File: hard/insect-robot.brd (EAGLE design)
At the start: 10.2 x 25.4 mm, 13 parts, among them Q1 AO3400, SW1 SWITCH-DT, U1 ATMEGA328P-QFN32, U2 PW0316

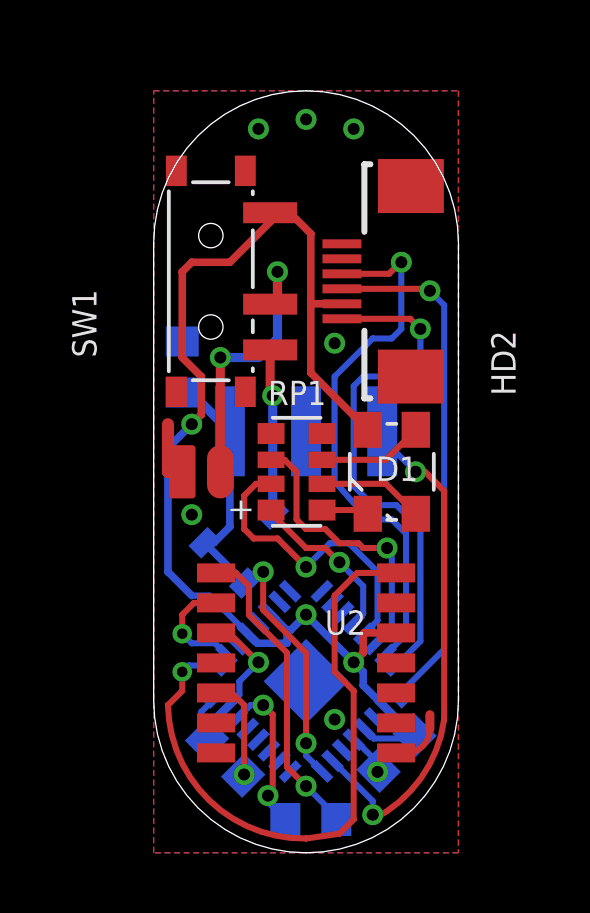
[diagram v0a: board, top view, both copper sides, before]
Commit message: Relocate some components
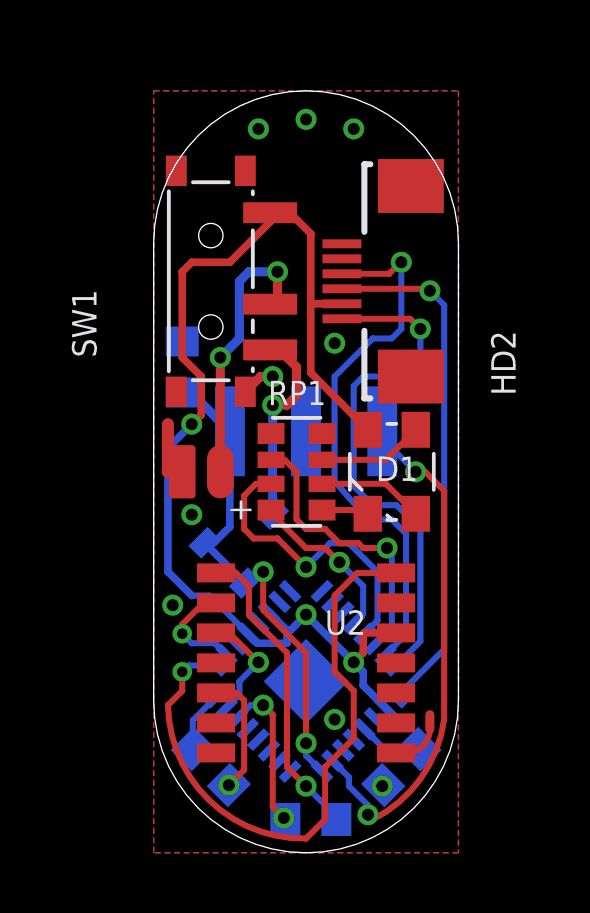
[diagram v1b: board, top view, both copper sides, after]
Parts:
- moved R2 0.57 mm to (1.91, 2.86)
- moved C1 0.50 mm to (8.26, 2.86)
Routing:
- net SWITCH-B: track 5.71 -> 6.83 mm
- net R-BCTS: track 3.51 -> 4.07 mm
- net LINK: track 21.2 -> 20.7 mm
- net GND: track 5.65 -> 5.44 mm, vias 7 -> 9

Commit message: Redesign
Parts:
- removed Q1: AO3400, MyLibrary:SOT23-0
- removed R3: 1kΩ, MyLibrary:SMD0603
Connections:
- removed net BAT-COM: BAT1.+, SW1.COM
- removed net SWITCH-B: Q1.3, SW1.B
- new net RST: HD2.5, U1.29
- new net VDD: D1.2, SW1.A, U1.18, U1.4, U1.6, U2.5
- net GND: no longer R3.2
- net L: now also HD1.1, U1.24; no longer HD1.3, U1.23
- net R: now also HD1.3, U1.23; no longer HD1.1, Q1.1, Q1.2, R3.1, U1.24
- net VBAT: now also BAT1.+, SW1.COM; no longer D1.2, SW1.A, U1.18, U1.4, U1.6, U2.5
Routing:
- net VDD: track 0.00 -> 37.2 mm, vias 0 -> 4
- net VBAT: track 38.2 -> 9.20 mm, vias 3 -> 2
- net BAT-COM: track 9.20 -> 0.00 mm, vias 2 -> 0
- net SWITCH-B: track 6.83 -> 0.00 mm, vias 1 -> 0
- net L: track 17.2 -> 12.6 mm
- net MISO: track 17.5 -> 14.6 mm
- net R: track 16.5 -> 17.9 mm
- net GND: track 5.44 -> 4.31 mm, vias 9 -> 7

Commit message: Redesign finished
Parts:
- D1: value LED-RGB-A-3528 -> LED-RGB-A-0603; device MyLibrary:3528-4 -> MyLibrary:LED-0603X2
- moved D1 11.5 mm to (5.08, 23.8)
- moved RP1 0.63 mm to (5.40, 12.7), turned to 0 degrees
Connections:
- net B-: now also D1.4, RP1.7; no longer D1.3, RP1.3
- net G-: now also D1.2; no longer D1.4
- net R-: now also RP1.3; no longer RP1.7
- net RB-: now also RP1.8; no longer RP1.4
- net RR-: now also RP1.4; no longer RP1.8
- net VDD: now also D1.3; no longer D1.2
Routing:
- net RST: track 0.00 -> 27.9 mm, vias 0 -> 3
- net R-: track 1.81 -> 11.5 mm, vias 0 -> 2
- net G-: track 3.54 -> 12.3 mm, vias 0 -> 2
- net B-: track 3.54 -> 11.3 mm, vias 0 -> 2
- net VDD: track 37.2 -> 32.1 mm
- net RG-: track 10.1 -> 6.29 mm
- net RB-: track 9.52 -> 6.60 mm
- net VBAT: track 9.20 -> 11.6 mm
- net MOSI: track 17.8 -> 16.4 mm
- net L: track 12.6 -> 13.7 mm
- net R-TX: track 10.6 -> 11.5 mm
- net R: track 17.9 -> 18.6 mm
- net GND: vias 7 -> 6

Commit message: Place labels
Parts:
- added OSHW: (no value), MyLibrary:ICON-OSHW
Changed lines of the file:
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@@
 </element>
 <element name="D1" library="MyLibrary" package="LED-0603X2" value="LED-RGB-A-0603" x="5.08" y="23.8125" smashed="yes" rot="R270">
-<attribute name="NAME" x="7.6075" y="23.9175" size="0.8128" layer="25" font="vector" rot="R90"/>
+<attribute name="NAME" x="5.185" y="21.6025" size="0.8128" layer="25" font="vector"/>
 <attribute name="VALUE" x="2.68" y="25.6125" size="0.8128" layer="27" font="vector" rot="R270"/>
 </element>
@@
 <attribute name="VALUE" x="6.876053125" y="10.205125" size="0.8128" layer="28" font="vector" rot="MR225"/>
 </element>
-<element name="U2" library="MyLibrary" package="PW0316" value="PW0316" x="5.08" y="5.08" rot="R180"/>
-<element name="HD2" library="MyLibrary" package="FPC0.5-6-DRAWER" value="HEADER1X6-SS-FPC0.5-DRAWER" x="9.525" y="19.05" rot="R90"/>
-<element name="SW1" library="MyLibrary" package="SWITCH-SMD-6.7X2.7" value="SWITCH-DT" x="1.905" y="19.05"/>
+<element name="U2" library="MyLibrary" package="PW0316" value="PW0316" x="5.08" y="5.08" smashed="yes" rot="R180">
+<attribute name="NAME" x="6.2075" y="9.3025" size="0.8128" layer="25" font="vector" rot="R270"/>
+<attribute name="VALUE" x="7.08" y="9.08" size="0.8128" layer="27" font="vector" rot="R180"/>
+</element>
+<element name="HD2" library="MyLibrary" package="FPC0.5-6-DRAWER" value="HEADER1X6-SS-FPC0.5-DRAWER" x="9.525" y="19.05" smashed="yes" rot="R90">
+<attribute name="NAME" x="7.62" y="20.32" size="0.8128" layer="25" font="vector" rot="R270"/>
+<attribute name="VALUE" x="13.335" y="15.24" size="0.8128" layer="27" font="vector" rot="R90"/>
+</element>
+<element name="SW1" library="MyLibrary" package="SWITCH-SMD-6.7X2.7" value="SWITCH-DT" x="1.905" y="19.05" smashed="yes">
+<attribute name="NAME" x="2.8575" y="18.0975" size="0.8128" layer="25" font="vector" ratio="11" rot="R90"/>
+<attribute name="VALUE" x="-0.635" y="16.51" size="0.8128" layer="27" font="vector" ratio="11" rot="R90"/>
+</element>
+<element name="OSHW" library="MyLibrary" package="ICON-OSHW" value="" x="5.08" y="20.955" rot="MR0"/>
 </elements>
 <signals>

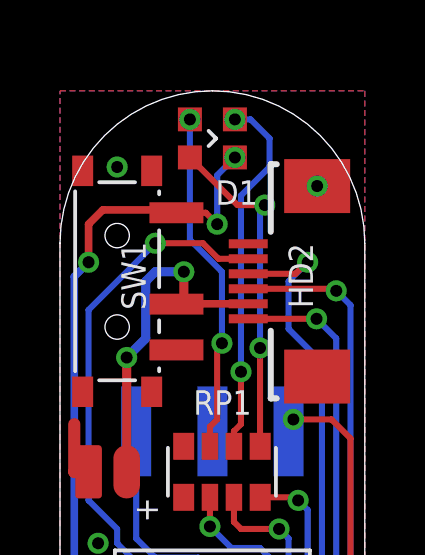
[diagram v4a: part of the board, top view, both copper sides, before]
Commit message: Fixed RGB LED footprint
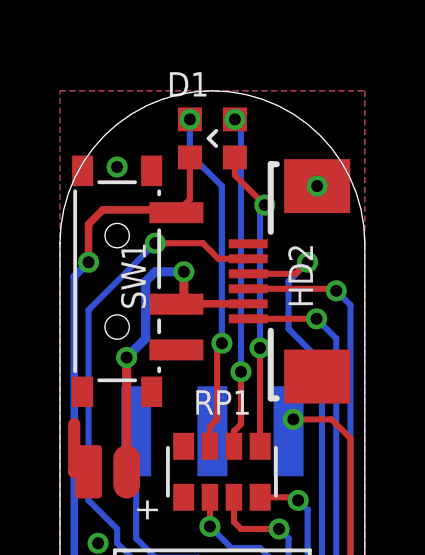
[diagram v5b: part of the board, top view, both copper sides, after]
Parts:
- turned D1 to 90 degrees
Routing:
- net VDD: track 32.1 -> 30.2 mm, vias 4 -> 2
- net G-: track 12.3 -> 11.1 mm
- net B-: track 11.3 -> 10.1 mm
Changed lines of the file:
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@@
 <setting verticaltext="up"/>
 </settings>
-<grid distance="0.0125" unitdist="inch" unit="mm" style="lines" multiple="1" display="yes" altdistance="0.00625" altunitdist="inch" altunit="inch"/>
+<grid distance="0.0125" unitdist="inch" unit="inch" style="lines" multiple="1" display="yes" altdistance="0.00625" altunitdist="inch" altunit="inch"/>
 <layers>
 <layer number="1" name="Top" color="4" fill="1" visible="yes" active="yes"/>
@@
 <attribute name="VALUE" x="6.45895" y="2.8575" size="0.6096" layer="28" font="vector" rot="MR135"/>
 </element>
-<element name="D1" library="MyLibrary" package="LED-0603X2" value="LED-RGB-A-0603" x="5.08" y="23.8125" smashed="yes" rot="R270">
-<attribute name="NAME" x="5.185" y="21.6025" size="0.8128" layer="25" font="vector"/>
-<attribute name="VALUE" x="2.68" y="25.6125" size="0.8128" layer="27" font="vector" rot="R270"/>
+<element name="D1" library="MyLibrary" package="LED-0603X2" value="LED-RGB-A-0603" x="5.08" y="23.8125" smashed="yes" rot="R90">
+<attribute name="NAME" x="4.975" y="26.0225" size="0.8128" layer="25" font="vector" rot="R180"/>
+<attribute name="VALUE" x="7.48" y="22.0125" size="0.8128" layer="27" font="vector" rot="R90"/>
 </element>
 <element name="HD1" library="MyLibrary" package="SMD-1X3-LYING" value="HEADER1X3-SMD-LYING" x="8.89" y="19.05" rot="MR180"/>
@@
 <wire x1="0.9525" y1="19.685" x2="0.47625" y2="19.20875" width="0.254" layer="16"/>
 <wire x1="0.47625" y1="19.20875" x2="0.47625" y2="9.36625" width="0.254" layer="16"/>
-<wire x1="3.883" y1="21.336" x2="4.85775" y2="21.336" width="0.2032" layer="1"/>
-<wire x1="4.85775" y1="21.336" x2="5.23875" y2="20.955" width="0.2032" layer="1"/>
-<via x="5.23875" y="20.955" extent="1-16" drill="0.4"/>
-<wire x1="5.23875" y1="20.955" x2="5.23875" y2="22.58625" width="0.2032" layer="16"/>
-<wire x1="5.23875" y1="22.58625" x2="5.83" y2="23.1775" width="0.2032" layer="16"/>
-<via x="5.83" y="23.1775" extent="1-16" drill="0.4"/>
+<wire x1="3.883" y1="21.336" x2="4.33" y2="21.783" width="0.2032" layer="1"/>
+<wire x1="4.33" y1="21.783" x2="4.33" y2="23.1775" width="0.2032" layer="1"/>
 </signal>
 <signal name="GND">
@@
 <via x="5.3975" y="16.98625" extent="1-16" drill="0.4"/>
 <via x="4.33" y="24.4475" extent="1-16" drill="0.4"/>
-<wire x1="5.3975" y1="16.98625" x2="5.3975" y2="19.3675" width="0.2032" layer="16"/>
-<wire x1="5.3975" y1="19.3675" x2="4.33" y2="20.435" width="0.2032" layer="16"/>
-<wire x1="4.33" y1="20.435" x2="4.33" y2="24.4475" width="0.2032" layer="16"/>
+<wire x1="5.3975" y1="16.98625" x2="5.3975" y2="22.225" width="0.2032" layer="16"/>
+<wire x1="5.3975" y1="22.225" x2="4.33" y2="23.2925" width="0.2032" layer="16"/>
+<wire x1="4.33" y1="23.2925" x2="4.33" y2="24.4475" width="0.2032" layer="16"/>
 </signal>
 <signal name="G-">
@@
 <wire x1="5.7975" y1="13.55" x2="5.7975" y2="14.0525" width="0.2032" layer="1"/>
 <wire x1="5.7975" y1="14.0525" x2="6.0325" y2="14.2875" width="0.2032" layer="1"/>
-<wire x1="5.715" y1="24.3325" x2="5.83" y2="24.4475" width="0.2032" layer="16"/>
 <via x="5.83" y="24.4475" extent="1-16" drill="0.4"/>
 <wire x1="6.0325" y1="14.2875" x2="6.0325" y2="16.03375" width="0.2032" layer="1"/>
 <via x="6.0325" y="16.03375" extent="1-16" drill="0.4"/>
-<wire x1="6.0325" y1="16.03375" x2="6.0325" y2="21.9075" width="0.2032" layer="16"/>
-<wire x1="6.0325" y1="21.9075" x2="6.985" y2="22.86" width="0.2032" layer="16"/>
-<wire x1="6.985" y1="22.86" x2="6.985" y2="23.8125" width="0.2032" layer="16"/>
-<wire x1="6.985" y1="23.8125" x2="6.35" y2="24.4475" width="0.2032" layer="16"/>
-<wire x1="6.35" y1="24.4475" x2="5.83" y2="24.4475" width="0.2032" layer="16"/>
+<wire x1="6.0325" y1="16.03375" x2="6.0325" y2="24.245" width="0.2032" layer="16"/>
+<wire x1="6.0325" y1="24.245" x2="5.83" y2="24.4475" width="0.2032" layer="16"/>
 </signal>
 <signal name="B-">
@@
 <wire x1="6.6675" y1="21.43125" x2="6.82625" y2="21.59" width="0.2032" layer="16"/>
 <via x="6.82625" y="21.59" extent="1-16" drill="0.4"/>
-<wire x1="6.82625" y1="21.59" x2="5.9175" y2="21.59" width="0.2032" layer="1"/>
-<wire x1="5.9175" y1="21.59" x2="4.33" y2="23.1775" width="0.2032" layer="1"/>
+<wire x1="6.82625" y1="21.59" x2="5.83" y2="22.58625" width="0.2032" layer="1"/>
+<wire x1="5.83" y1="22.58625" x2="5.83" y2="23.1775" width="0.2032" layer="1"/>
 </signal>
 <signal name="RST">

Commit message: PWM pins
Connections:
- removed net MOSI: HD2.4, U1.15
- removed net RB-: RP1.8, U1.14
- new net RB-/MOSI: HD2.4, RP1.8, U1.15
- net L: now also U1.14
- net R: now also U1.13
- net RG-: now also U1.10; no longer U1.13
- net RR-: now also U1.9; no longer U1.12
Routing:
- net RB-/MOSI: track 0.00 -> 18.6 mm, vias 0 -> 2
- net MOSI: track 16.4 -> 0.00 mm, vias 1 -> 0
- net L: track 13.7 -> 23.6 mm
- net RB-: track 6.60 -> 0.00 mm, vias 1 -> 0
- net R: track 18.6 -> 24.8 mm, vias 2 -> 3
- net RG-: track 6.29 -> 4.14 mm
- net RR-: track 5.70 -> 3.73 mm
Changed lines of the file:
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@@
 <contactref element="HD1" pad="1"/>
 <contactref element="U1" pad="24"/>
-<wire x1="2.54" y1="10.4775" x2="2.54" y2="14.05" width="0.2032" layer="16"/>
-<wire x1="2.54" y1="10.4775" x2="3.175" y2="9.8425" width="0.2032" layer="16"/>
+<wire x1="2.54" y1="12.065" x2="2.54" y2="14.05" width="0.2032" layer="16"/>
 <via x="5.55625" y="3.96875" extent="1-16" drill="0.4"/>
 <wire x1="5.55625" y1="4.60375" x2="5.08" y2="5.08" width="0.2032" layer="1"/>
-<wire x1="5.08" y1="5.08" x2="5.08" y2="9.36625" width="0.2032" layer="1"/>
-<via x="5.08" y="9.36625" extent="1-16" drill="0.4"/>
-<wire x1="5.08" y1="9.36625" x2="4.60375" y2="9.8425" width="0.2032" layer="16"/>
-<wire x1="4.60375" y1="9.8425" x2="3.175" y2="9.8425" width="0.2032" layer="16"/>
 <wire x1="5.55625" y1="4.60375" x2="5.55625" y2="3.96875" width="0.2032" layer="1"/>
 <wire x1="5.55625" y1="3.96875" x2="5.23875" y2="3.65125" width="0.2032" layer="16"/>
 <wire x1="5.23875" y1="3.65125" x2="5.23875" y2="3.081375" width="0.2032" layer="16"/>
 <wire x1="5.23875" y1="3.081375" x2="5.61033125" y2="2.70979375" width="0.2032" layer="16"/>
+<contactref element="U1" pad="14"/>
+<wire x1="7.3781" y1="6.952434375" x2="8.09625" y2="7.670584375" width="0.2032" layer="16"/>
+<wire x1="7.3025" y1="11.7475" x2="2.8575" y2="11.7475" width="0.2032" layer="16"/>
+<wire x1="2.8575" y1="11.7475" x2="2.54" y2="12.065" width="0.2032" layer="16"/>
+<wire x1="5.08" y1="5.08" x2="5.08" y2="9.2075" width="0.2032" layer="1"/>
+<wire x1="5.08" y1="9.2075" x2="4.1275" y2="10.16" width="0.2032" layer="1"/>
+<wire x1="4.1275" y1="10.16" x2="3.4925" y2="10.16" width="0.2032" layer="1"/>
+<wire x1="3.4925" y1="10.16" x2="3.175" y2="10.4775" width="0.2032" layer="1"/>
+<via x="3.175" y="10.4775" extent="1-16" drill="0.4"/>
+<wire x1="3.175" y1="10.4775" x2="2.54" y2="11.1125" width="0.2032" layer="16"/>
+<wire x1="2.54" y1="11.1125" x2="2.54" y2="12.065" width="0.2032" layer="16"/>
+<wire x1="8.09625" y1="7.670584375" x2="8.09625" y2="10.95375" width="0.2032" layer="16"/>
+<wire x1="8.09625" y1="10.95375" x2="7.3025" y2="11.7475" width="0.2032" layer="16"/>
 </signal>
 <signal name="R">
@@
 <wire x1="6.50875" y1="2.51848125" x2="5.963884375" y2="3.063346875" width="0.2032" layer="16"/>
 <via x="7.77875" y="14.44625" extent="1-16" drill="0.4"/>
-<wire x1="9.68375" y1="4.445" x2="9.68375" y2="13.81125" width="0.2032" layer="1"/>
+<wire x1="9.68375" y1="4.445" x2="9.68375" y2="11.1125" width="0.2032" layer="1"/>
+<wire x1="9.68375" y1="11.1125" x2="9.68375" y2="13.81125" width="0.2032" layer="1"/>
 <wire x1="9.68375" y1="13.81125" x2="9.04875" y2="14.44625" width="0.2032" layer="1"/>
 <wire x1="9.04875" y1="14.44625" x2="7.77875" y2="14.44625" width="0.2032" layer="1"/>
 <wire x1="7.77875" y1="14.44625" x2="7.62" y2="14.2875" width="0.2032" layer="16"/>
 <wire x1="7.62" y1="14.2875" x2="7.62" y2="14.05" width="0.2032" layer="16"/>
+<contactref element="U1" pad="13"/>
+<wire x1="7.02454375" y1="7.3059875" x2="7.46125" y2="7.74269375" width="0.2032" layer="16"/>
+<wire x1="7.46125" y1="10.4775" x2="7.3025" y2="10.63625" width="0.2032" layer="16"/>
+<via x="7.3025" y="10.63625" extent="1-16" drill="0.4"/>
+<wire x1="7.3025" y1="10.63625" x2="7.46125" y2="10.795" width="0.2032" layer="1"/>
+<wire x1="7.46125" y1="10.795" x2="9.36625" y2="10.795" width="0.2032" layer="1"/>
+<wire x1="9.36625" y1="10.795" x2="9.68375" y2="11.1125" width="0.2032" layer="1"/>
+<wire x1="7.46125" y1="7.74269375" x2="7.46125" y2="10.4775" width="0.2032" layer="16"/>
 </signal>
 <signal name="RXD">
@@
 <wire x1="5.715" y1="1.11125" x2="5.08" y2="0.47625" width="0.2032" layer="1"/>
 </signal>
-<signal name="MOSI">
+<signal name="RB-/MOSI">
 <contactref element="U1" pad="15"/>
 <contactref element="HD2" pad="4"/>
@@
 <wire x1="7.62" y1="17.4625" x2="7.62" y2="19.05" width="0.2032" layer="16"/>
 <wire x1="7.62" y1="19.05" x2="8.255" y2="19.685" width="0.2032" layer="16"/>
-<wire x1="8.73125" y1="7.598478125" x2="8.73125" y2="16.35125" width="0.2032" layer="16"/>
 <wire x1="8.73125" y1="16.35125" x2="7.62" y2="17.4625" width="0.2032" layer="16"/>
+<contactref element="RP1" pad="8"/>
+<wire x1="6.6725" y1="11.85" x2="6.775" y2="11.7475" width="0.2032" layer="1"/>
+<wire x1="6.775" y1="11.7475" x2="8.41375" y2="11.7475" width="0.2032" layer="1"/>
+<via x="8.41375" y="11.7475" extent="1-16" drill="0.4"/>
+<wire x1="8.73125" y1="7.598478125" x2="8.73125" y2="11.43" width="0.2032" layer="16"/>
+<wire x1="8.73125" y1="11.43" x2="8.73125" y2="16.35125" width="0.2032" layer="16"/>
+<wire x1="8.41375" y1="11.7475" x2="8.73125" y2="11.43" width="0.2032" layer="16"/>
 </signal>
 <signal name="MISO">
@@
 <wire x1="6.275" y1="18.3" x2="3.895" y2="18.3" width="0.254" layer="1"/>
 <wire x1="3.895" y1="18.3" x2="3.883" y2="18.288" width="0.254" layer="1"/>
-</signal>
-<signal name="RR-">
-<contactref element="U1" pad="12"/>
-<contactref element="RP1" pad="4"/>
-<wire x1="6.670990625" y1="7.659540625" x2="6.985" y2="7.97355" width="0.2032" layer="16"/>
-<wire x1="6.985" y1="7.97355" x2="6.985" y2="9.8425" width="0.2032" layer="16"/>
-<wire x1="6.985" y1="9.8425" x2="6.6675" y2="10.16" width="0.2032" layer="16"/>
-<wire x1="6.6675" y1="10.16" x2="5.715" y2="10.16" width="0.2032" layer="16"/>
-<wire x1="5.715" y1="10.16" x2="4.9975" y2="10.8775" width="0.2032" layer="16"/>
-<via x="4.9975" y="10.8775" extent="1-16" drill="0.4"/>
-<wire x1="4.9975" y1="10.8775" x2="4.9975" y2="11.85" width="0.2032" layer="1"/>
-</signal>
-<signal name="RG-">
-<contactref element="U1" pad="13"/>
-<contactref element="RP1" pad="6"/>
-<wire x1="7.02454375" y1="7.3059875" x2="7.62" y2="7.90144375" width="0.2032" layer="16"/>
-<wire x1="7.62" y1="7.90144375" x2="7.62" y2="10.4775" width="0.2032" layer="16"/>
-<wire x1="7.62" y1="10.4775" x2="7.3025" y2="10.795" width="0.2032" layer="16"/>
-<via x="7.3025" y="10.795" extent="1-16" drill="0.4"/>
-<wire x1="7.3025" y1="10.795" x2="6.0325" y2="10.795" width="0.2032" layer="1"/>
-<wire x1="6.0325" y1="10.795" x2="5.7975" y2="11.03" width="0.2032" layer="1"/>
-<wire x1="5.7975" y1="11.03" x2="5.7975" y2="11.85" width="0.2032" layer="1"/>
-</signal>
-<signal name="RB-">
-<contactref element="U1" pad="14"/>
-<contactref element="RP1" pad="8"/>
-<wire x1="7.3781" y1="6.952434375" x2="8.255" y2="7.829334375" width="0.2032" layer="16"/>
-<wire x1="8.255" y1="7.829334375" x2="8.255" y2="11.43" width="0.2032" layer="16"/>
-<wire x1="8.255" y1="11.43" x2="7.9375" y2="11.7475" width="0.2032" layer="16"/>
-<via x="7.9375" y="11.7475" extent="1-16" drill="0.4"/>
-<wire x1="7.9375" y1="11.7475" x2="7.835" y2="11.85" width="0.2032" layer="1"/>
-<wire x1="7.835" y1="11.85" x2="6.6725" y2="11.85" width="0.2032" layer="1"/>
 </signal>
 <signal name="R-">
@@
 <wire x1="0.9525" y1="11.7475" x2="0.9525" y2="18.0975" width="0.2032" layer="16"/>
 </signal>
+<signal name="RR-">
+<contactref element="RP1" pad="4"/>
+<contactref element="U1" pad="9"/>
+<wire x1="4.9975" y1="10.8775" x2="6.0325" y2="9.8425" width="0.2032" layer="16"/>
+<wire x1="6.0325" y1="9.8425" x2="6.0325" y2="9.142371875" width="0.2032" layer="16"/>
+<wire x1="6.0325" y1="9.142371875" x2="5.61033125" y2="8.720203125" width="0.2032" layer="16"/>
+<via x="4.9975" y="10.8775" extent="1-16" drill="0.4"/>
+<wire x1="4.9975" y1="10.8775" x2="4.9975" y2="11.85" width="0.2032" layer="1"/>
+</signal>
+<signal name="RG-">
+<contactref element="RP1" pad="6"/>
+<contactref element="U1" pad="10"/>
+<wire x1="5.963884375" y1="8.36665" x2="6.6675" y2="9.070265625" width="0.2032" layer="16"/>
+<wire x1="5.7975" y1="11.03" x2="5.7975" y2="11.85" width="0.2032" layer="1"/>
+<wire x1="6.6675" y1="9.070265625" x2="6.6675" y2="10.16" width="0.2032" layer="16"/>
+<wire x1="6.6675" y1="10.16" x2="6.0325" y2="10.795" width="0.2032" layer="16"/>
+<via x="6.0325" y="10.795" extent="1-16" drill="0.4"/>
+<wire x1="6.0325" y1="10.795" x2="5.7975" y2="11.03" width="0.2032" layer="1"/>
+</signal>
 </signals>
